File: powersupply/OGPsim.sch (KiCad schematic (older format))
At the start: 31 parts, among them Q1 Q_NPN_BEC, Q2 Q_NPN_BEC, Q5 Q_NPN_BEC, U1 LM317_TO39

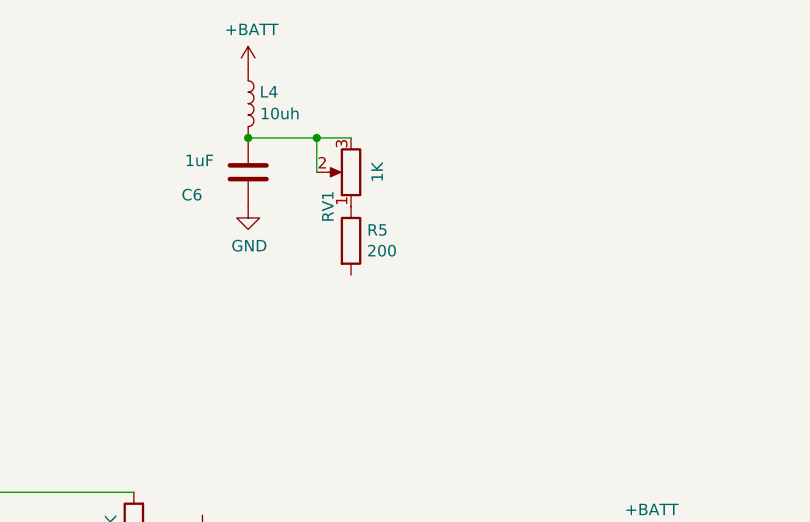
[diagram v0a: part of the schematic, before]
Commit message: Updated power supply board layout.
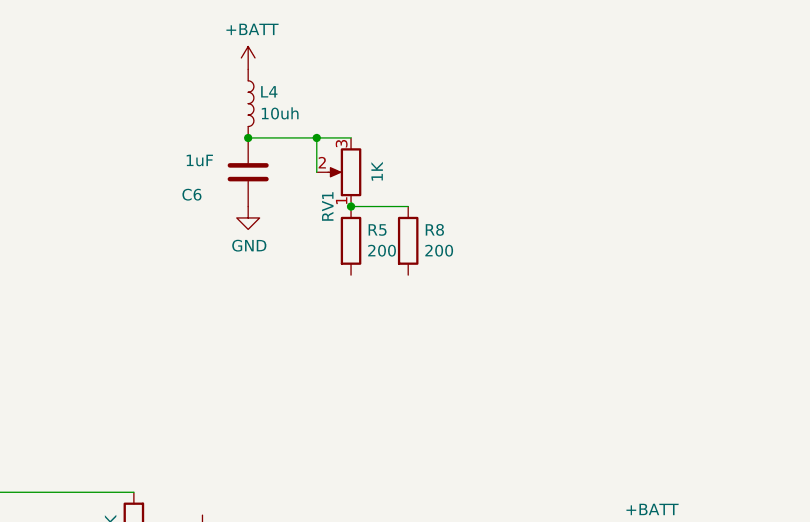
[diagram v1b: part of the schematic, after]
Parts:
- added R8: 200, Resistors_SMD:R_0402, symbol Device:R
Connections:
- net at R5.1, RV1.1: now also R8.1
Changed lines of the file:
@@
 	2850 4000 2850 4200
 Connection ~ 2850 4200
+$Comp
+L Device:R R8
+U 1 1 6128484D
+P 4950 2900
+F 0 "R8" H 5020 2946 50  0000 L CNN
+F 1 "200" H 5020 2855 50  0000 L CNN
+F 2 "Resistors_SMD:R_0402" V 4880 2900 50  0001 C CNN
+F 3 "~" H 4950 2900 50  0001 C CNN
+F 4 "https://www.digikey.com/en/products/detail/delta-electronics-cyntec/PFR05S-201-FNH/9761549" H 4950 2900 50  0001 C CNN "DigikeyLink"
+F 5 "2037-PFR05S-201-FNHCT-ND" H 4950 2900 50  0001 C CNN "DigikeyPart"
+	1    4950 2900
+	1    0    0    -1
+$EndComp
+Wire Wire Line
+	4950 2750 4700 2750
+Connection ~ 4700 2750
 $EndSCHEMATC

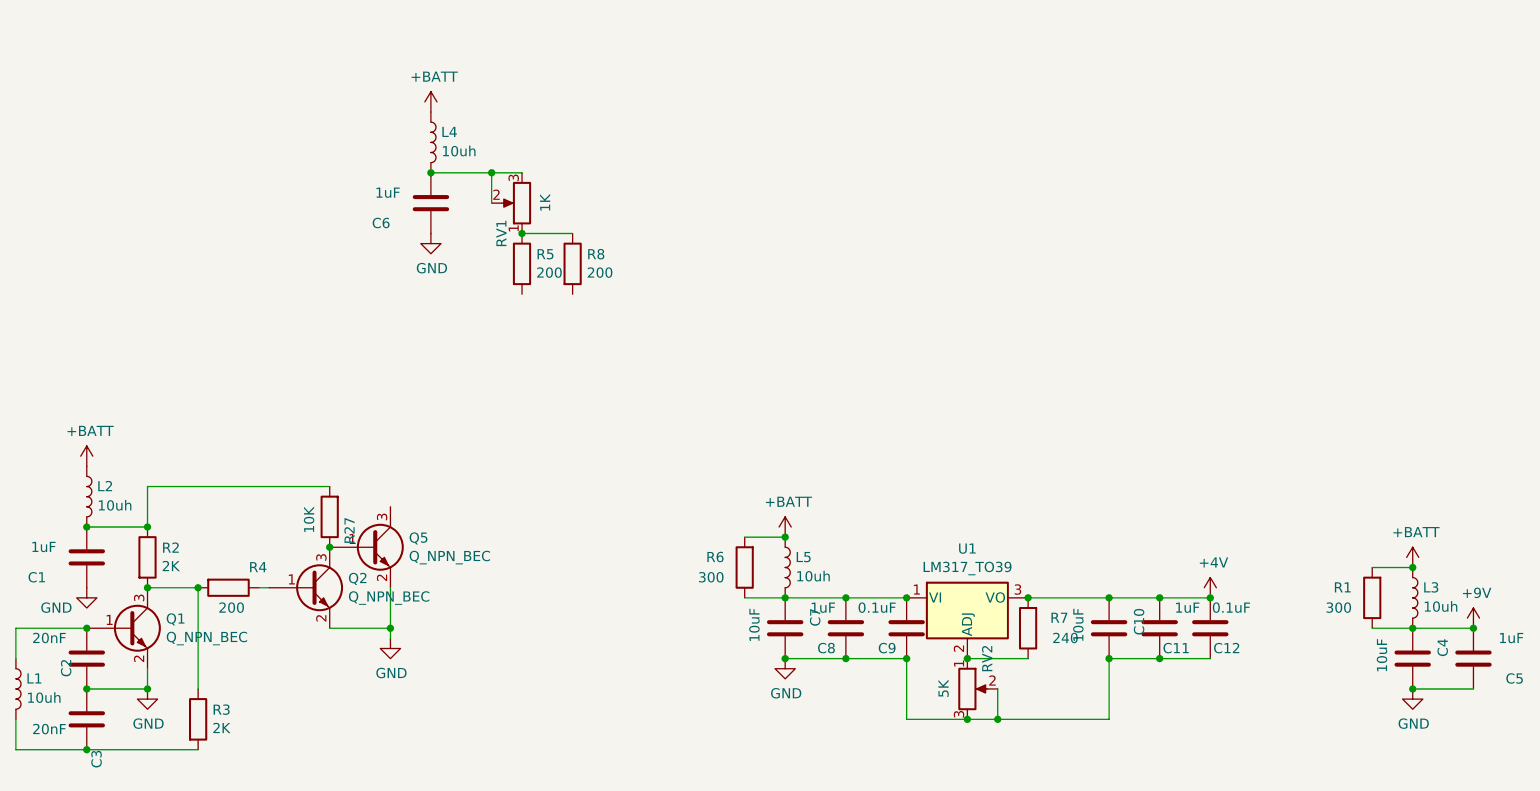
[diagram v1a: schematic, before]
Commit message: Updated power supply board and schematic to have solderable pads.
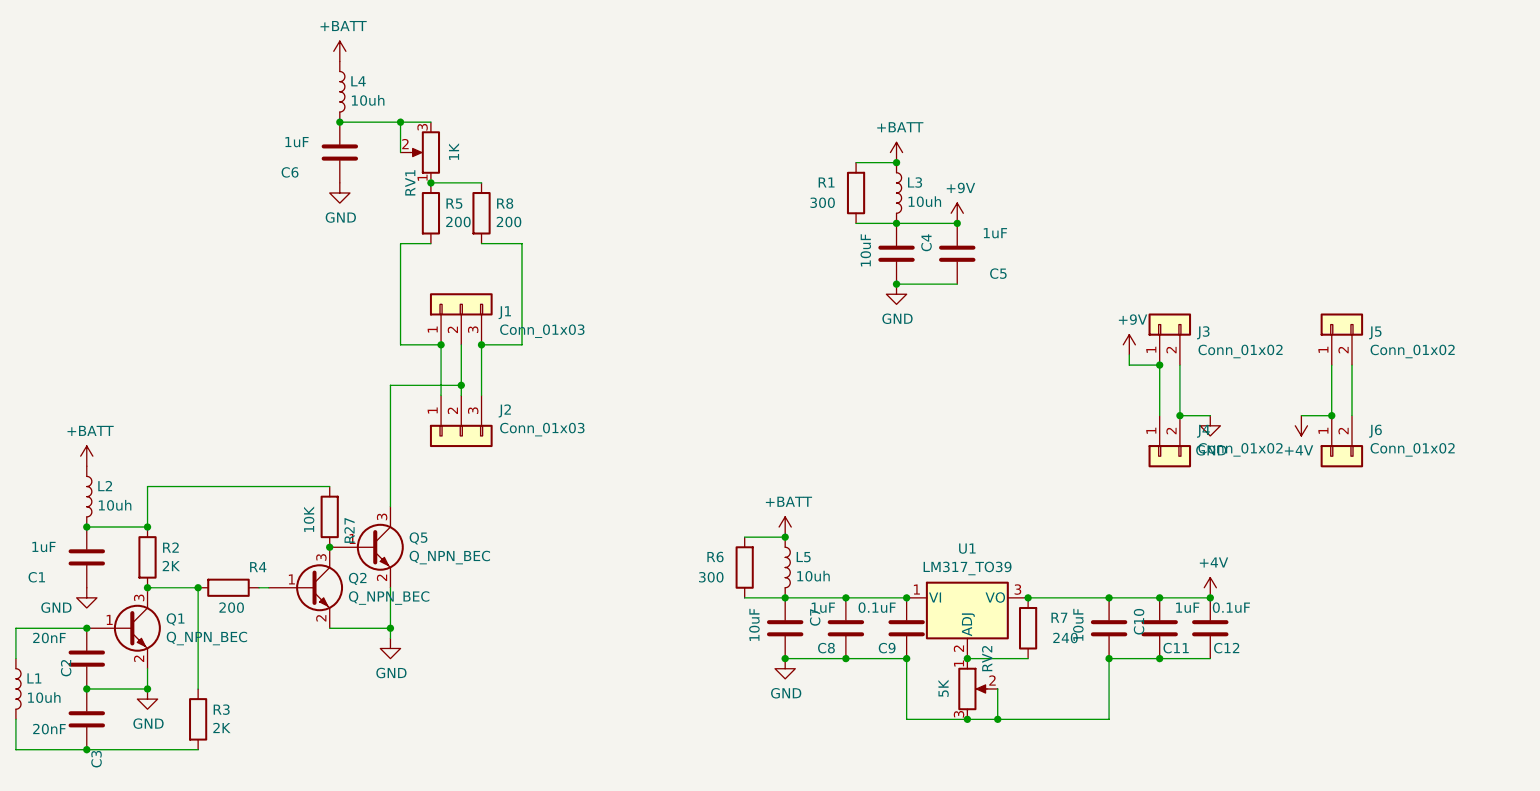
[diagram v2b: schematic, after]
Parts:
- added J1, J2: Conn_01x03, Connect:GS3, symbol Connector_Generic:Conn_01x03
- added J3, J4, J5, J6: Conn_01x02, Connect:GS2, symbol Connector_Generic:Conn_01x02
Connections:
- net +4V: now also J5.1 (Pin_1), J6.1 (Pin_1)
- net +9V: now also J3.1 (Pin_1), J4.1 (Pin_1)
- net GND: now also J3.2 (Pin_2), J4.2 (Pin_2)
- net at R5.2: now also J1.1 (Pin_1), J2.1 (Pin_1)
- net at R8.2: now also J1.3 (Pin_3), J2.3 (Pin_3)
- net at Q5.3 (C): now also J1.2 (Pin_2), J2.2 (Pin_2)
- new net: J5.2 (Pin_2), J6.2 (Pin_2)
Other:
- moved on the sheet: C4, C5, C6, L3, L4, R1, R5, R8, RV1

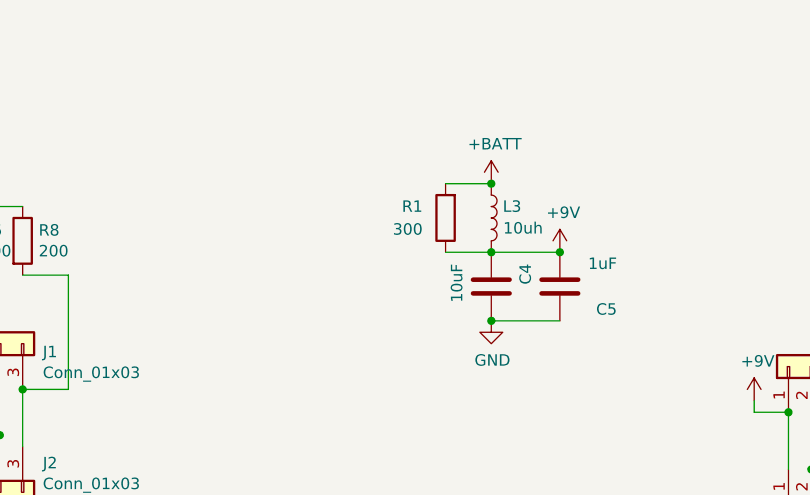
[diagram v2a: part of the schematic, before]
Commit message: Added TODO list. Added solder pads for power input on power supply board.
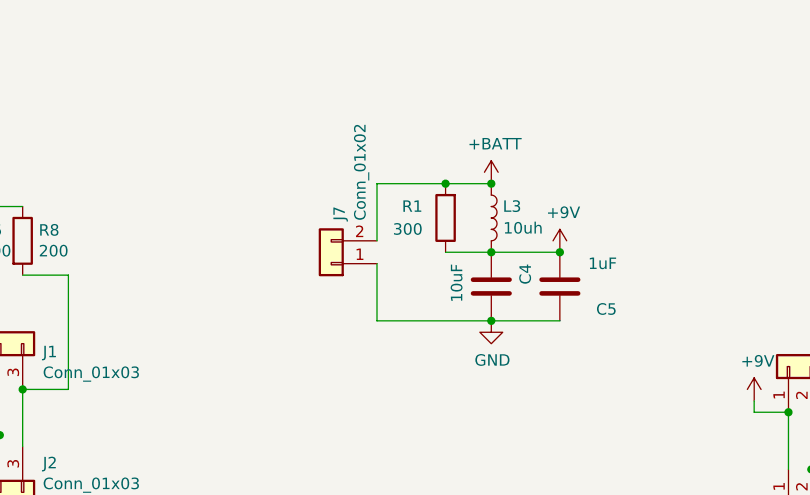
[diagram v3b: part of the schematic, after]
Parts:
- added J7: Conn_01x02, Connect:GS2, symbol Connector_Generic:Conn_01x02
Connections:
- net +BATT: now also J7.2 (Pin_2)
- net GND: now also J7.1 (Pin_1)
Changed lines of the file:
@@
 	8550 3650 8700 3650
 Connection ~ 8700 3650
+$Comp
+L Connector_Generic:Conn_01x02 J7
+U 1 1 61284E9C
+P 5850 2750
+F 0 "J7" V 5814 2562 50  0000 R CNN
+F 1 "Conn_01x02" V 5723 2562 50  0000 R CNN
+F 2 "Connect:GS2" H 5850 2750 50  0001 C CNN
+F 3 "~" H 5850 2750 50  0001 C CNN
+	1    5850 2750
+	-1   0    0    1
+$EndComp
+Wire Wire Line
+	6050 2650 6050 2400
+Wire Wire Line
+	6050 2400 6350 2400
+Connection ~ 6350 2400
+Wire Wire Line
+	6550 3000 6050 3000
+Wire Wire Line
+	6050 3000 6050 2750
 $EndSCHEMATC

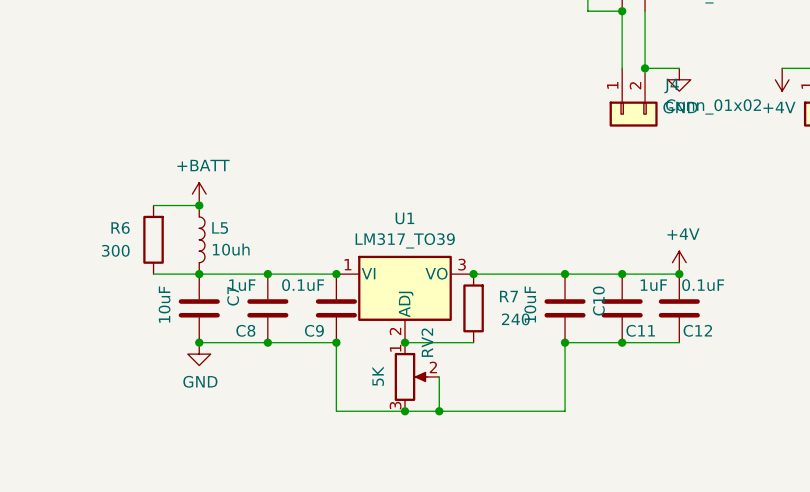
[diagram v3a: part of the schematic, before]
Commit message: Fixed LM317 having wrong pinout in schematic and on board layout.
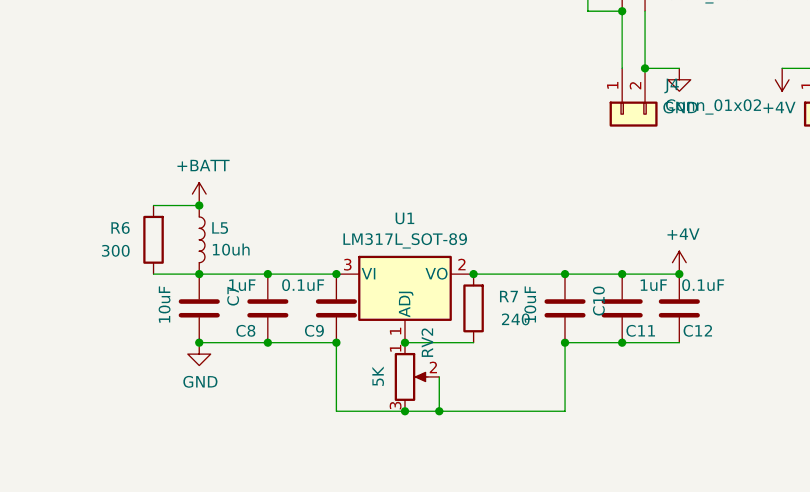
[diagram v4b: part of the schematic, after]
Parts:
- removed U1: LM317_TO39, TO_SOT_Packages_SMD:TO-252-2, symbol Regulator_Linear:LM317_TO39
- added U1: LM317L_SOT-89, TO_SOT_Packages_SMD:TO-252-2, symbol Regulator_Linear:LM317L_SOT-89
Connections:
- net +4V: now also U1.2 (VO)
- net at C7.2, C8.2, C9.2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: now also U1.3 (VI)
- net at R7.1, RV2.1: now also U1.1 (ADJ)
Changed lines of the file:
@@
 Connection ~ 6550 2400
-$Comp
-L Regulator_Linear:LM317_TO39 U1
-U 1 1 5ECF1E76
-P 6900 4550
-F 0 "U1" H 6900 4792 50  0000 C CNN
-F 1 "LM317_TO39" H 6900 4701 50  0000 C CNN
-F 2 "TO_SOT_Packages_SMD:TO-252-2" H 6900 4775 50  0001 C CIN
-F 3 "http://www.ti.com/lit/ds/symlink/lm317.pdf" H 6900 4550 50  0001 C CNN
-F 4 "https://www.digikey.com/en/products/detail/onsemi/LM317MABDTG/1476816" H 6900 4550 50  0001 C CNN "DigikeyLink"
-F 5 "LM317MABDTG-ND" H 6900 4550 50  0001 C CNN "DigikeyPart"
-	1    6900 4550
-	1    0    0    -1
-$EndComp
 $Comp
 L Device:R R7
@@
 	8100 4550 7850 4550
 Connection ~ 7850 4550
-Connection ~ 7200 4550
 Wire Wire Line
 	8100 4850 7850 4850
@@
 Wire Wire Line
 	6900 4850 7200 4850
-Connection ~ 6900 4850
 $Comp
 L Device:L L5
@@
 Wire Wire Line
 	6600 4550 6300 4550
-Connection ~ 6600 4550
 Connection ~ 6300 4550
 Wire Wire Line
@@
 Wire Wire Line
 	6050 3000 6050 2750
+$Comp
+L Regulator_Linear:LM317L_SOT-89 U1
+U 1 1 613EDE84
+P 6900 4550
+F 0 "U1" H 6900 4792 50  0000 C CNN
+F 1 "LM317L_SOT-89" H 6900 4701 50  0000 C CNN
+F 2 "TO_SOT_Packages_SMD:TO-252-2" H 6900 4800 50  0001 C CIN
+F 3 "http://www.ti.com/lit/ds/symlink/lm317l.pdf" H 6900 4550 50  0001 C CNN
+F 4 "https://www.digikey.com/en/products/detail/onsemi/LM317MABDTG/1476816" H 6900 4550 50  0001 C CNN "DigikeyLink"
+F 5 "LM317MABDTG-ND" H 6900 4550 50  0001 C CNN "DigikeyPart"
+	1    6900 4550
+	1    0    0    -1
+$EndComp
+Connection ~ 6900 4850
+Connection ~ 7200 4550
+Connection ~ 6600 4550
 $EndSCHEMATC
